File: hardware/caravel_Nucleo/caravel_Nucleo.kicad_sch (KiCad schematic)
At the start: 90 parts, among them J1 USB_B_Micro - 10118193-0001LF, J10 Conn_01x11_Female, J11 Conn_01x03, J12 Conn_01x02_Male, J2 Conn_01x02_Female, J3 Conn_01x02_Male, J4 Conn_01x04_Female, J5 Conn_01x02_Male, J6 Conn_01x02_Male, J7 Conn_01x06_Female, J8 Conn_01x03, J9 Conn_01x03, SW1 SW_Push - SKQGADE010, T1 Logo, T2 Logo, U1 FT232H, U10 MCP4661, U11 TAR5SxxU_SOT353F, U12 NUCLEO144-F429ZI, U2 SN74LVC1G125DCKR, U3 SN74LVC1G125DCKR, U4 MCP1319MT-29LE-OT, U5 TAR5SxxU_SOT353F, U6 TAR5SxxU_SOT353F, U7 W25Q32FVSS, U8 caravel_breakout, U9 MIC2211-AAYML-TR, X1 DSC6001_10MHZ, Y1 CSTNE12M0GH5L000R0

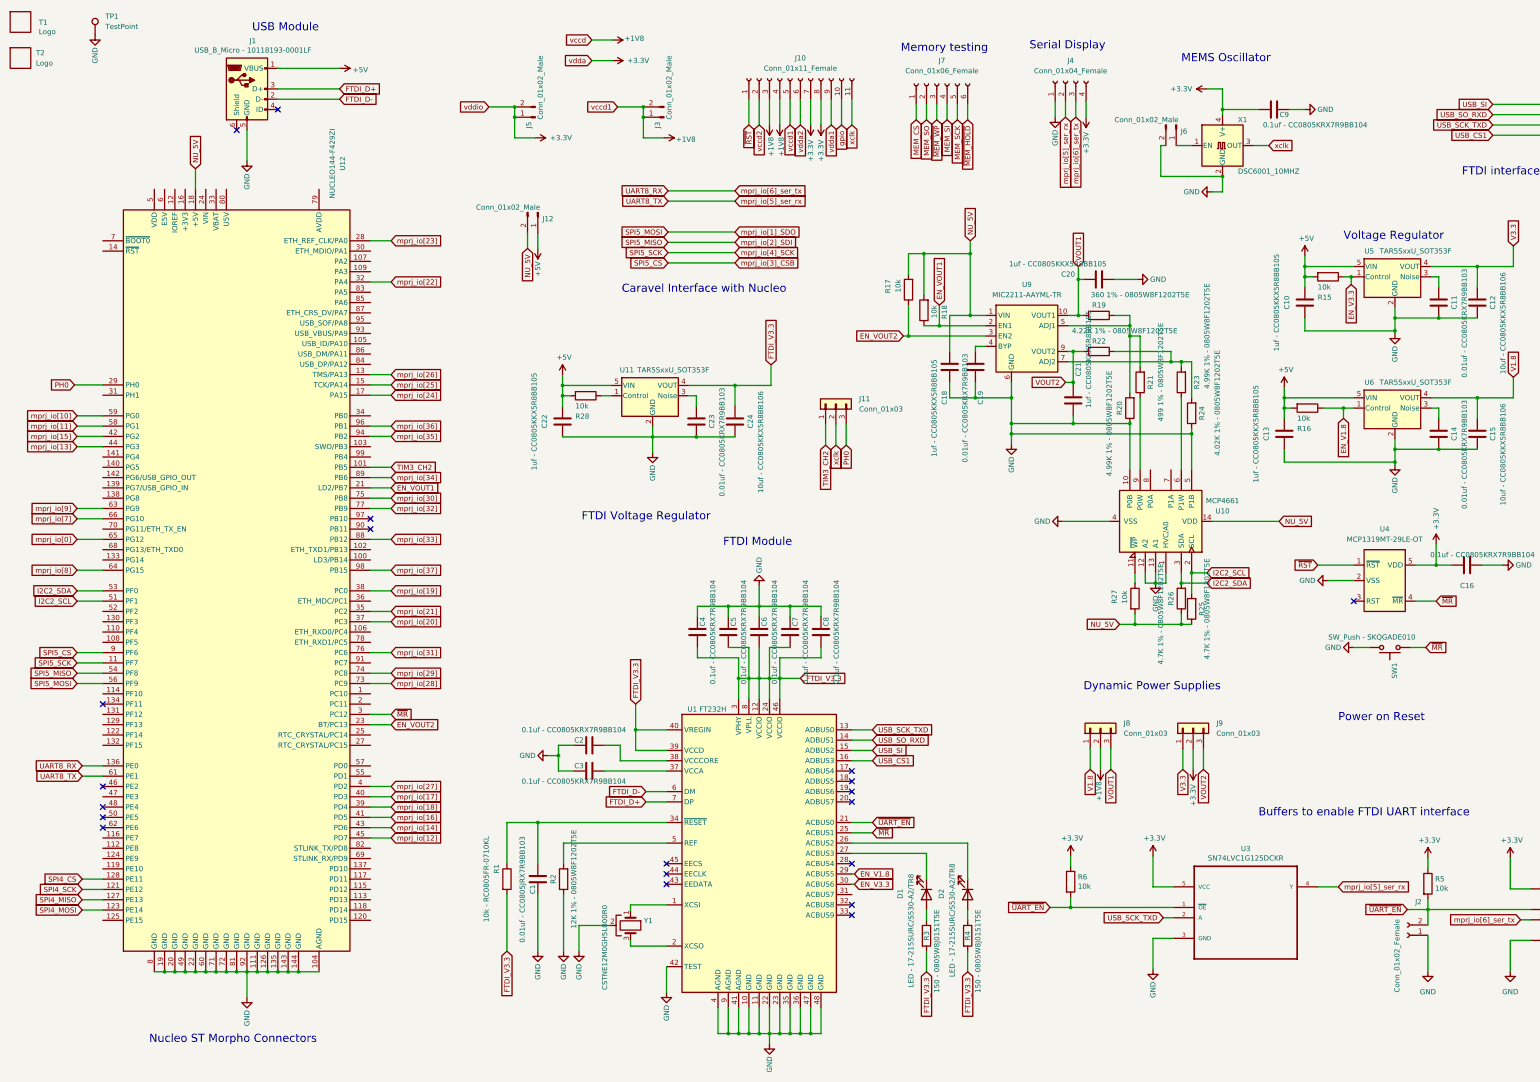
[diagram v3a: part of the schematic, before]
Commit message: update caravel nucleo hat board Rev A PCB
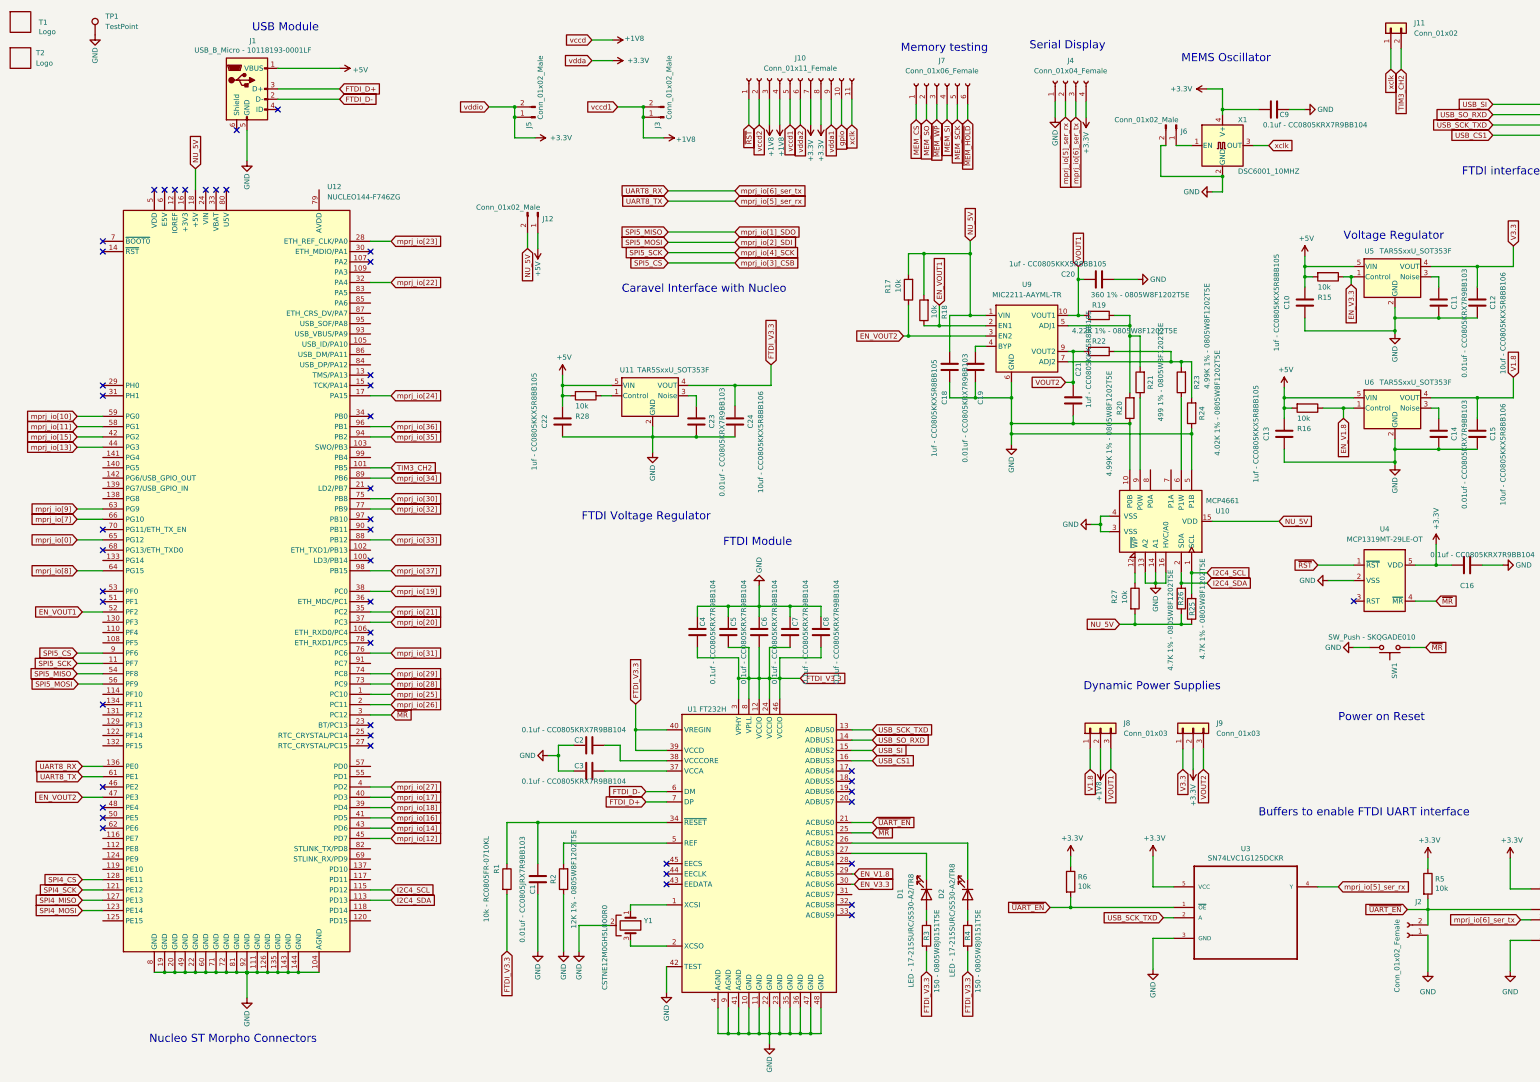
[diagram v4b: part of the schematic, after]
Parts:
- removed J11: Conn_01x03, Connector_PinHeader_2.54mm:PinHeader_1x03_P2.54mm_Vertical, symbol Connector_Generic:Conn_01x03
- removed U12: NUCLEO144-F429ZI, Caravel_Board:ST_Morpho_Connectors_144, symbol Caravel_board:NUCLEO144-F429ZI
- added J11: Conn_01x02, Connector_PinHeader_2.54mm:PinHeader_1x02_P2.54mm_Vertical, symbol Connector_Generic:Conn_01x02
- added U12: NUCLEO144-F746ZG, Module:ST_Morpho_Connector_144_STLink, symbol MCU_Module:NUCLEO144-F746ZG
- U10: footprint Caravel_Board:QFN-16-1EP_4x4mm_P0.65mm_EP2.5x2.5mm -> Package_DFN_QFN:QFN-16-1EP_5x5mm_P0.8mm_EP2.7x2.7mm
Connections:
- net EN_VOUT1: now also U12.52 (PF2)
- net EN_VOUT2: now also U12.47 (PE3)
- net GND: now also U10.14 (A1), U10.16 (HVC/A0), U10.3 (VSS), U12.104 (AGND), U12.111 (GND), U12.126 (GND), U12.135 (GND), U12.143 (GND), U12.144 (GND), U12.19 (GND), U12.20 (GND), U12.22 (GND), U12.49 (GND), U12.60 (GND), U12.71 (GND), U12.72 (GND), U12.8 (GND), U12.81 (GND), U12.92 (GND); no longer U10.1 (HVC/A0), U10.12 (A2)
- net NU_5V: now also U10.15 (VDD), U12.18 (+5V); no longer U10.14 (VDD)
- net SPI4_CS: now also U12.128 (PE11)
- net SPI4_MISO: now also U12.127 (PE13)
- net SPI4_MOSI: now also U12.123 (PE14)
- net SPI4_SCK: now also U12.121 (PE12)
- net SPI5_CS: now also U12.9 (PF6)
- net SPI5_MISO: now also U1.15 (ADBUS2), U8.41 (mprj_io[1]_SDO), U12.54 (PF8); no longer U1.14 (ADBUS1), U2.4 (Y), U8.40 (mprj_io[2]_SDI)
- net SPI5_MOSI: now also U1.14 (ADBUS1), U2.4 (Y), U8.40 (mprj_io[2]_SDI), U12.56 (PF9); no longer U1.15 (ADBUS2), U8.41 (mprj_io[1]_SDO)
- net SPI5_SCK: now also U12.11 (PF7)
- net TIM3_CH2: now also J11.2 (Pin_2), U12.101 (PB5)
- net UART8_RX: now also U12.136 (PE0)
- net UART8_TX: now also U12.61 (PE1)
- net mprj_io[0]: now also U12.65 (PG12)
- net mprj_io[10]: now also U12.59 (PG0)
- net mprj_io[11]: now also U12.58 (PG1)
- net mprj_io[12]: now also U12.45 (PD7)
- net mprj_io[13]: now also U12.44 (PG3)
- net mprj_io[14]: now also U12.43 (PD6)
- net mprj_io[15]: now also U12.42 (PG2)
- net mprj_io[16]: now also U12.41 (PD5)
- net mprj_io[17]: now also U12.40 (PD3)
- net mprj_io[18]: now also U12.39 (PD4)
- net mprj_io[19]: now also U12.38 (PC0)
- net mprj_io[20]: now also U12.37 (PC3)
- net mprj_io[21]: now also U12.35 (PC2)
- net mprj_io[22]: now also U12.32 (PA4)
- net mprj_io[23]: now also U12.28 (ETH_REF_CLK/PA0)
- net mprj_io[24]: now also U12.17 (PA15)
- net mprj_io[25]: now also U12.1 (PC10)
- net mprj_io[26]: now also U12.2 (PC11)
- net mprj_io[27]: now also U12.4 (PD2)
- net mprj_io[28]: now also U12.73 (PC9)
- net mprj_io[29]: now also U12.74 (PC8)
- net mprj_io[30]: now also U12.75 (PB8)
- net mprj_io[31]: now also U12.76 (PC6)
- net mprj_io[32]: now also U12.77 (PB9)
- net mprj_io[33]: now also U12.88 (PB12)
- net mprj_io[34]: now also U12.89 (PB6)
- net mprj_io[35]: now also U12.94 (PB2)
- net mprj_io[36]: now also U12.96 (PB1)
- net mprj_io[37]: now also U12.98 (PB15)
- net mprj_io[7]: now also U12.66 (PG10)
- net mprj_io[8]: now also U12.64 (PG15)
- net mprj_io[9]: now also U12.63 (PG9)
- net xclk: now also J11.1 (Pin_1)
- net ~{MR}: now also U12.3 (PC12)
- net at U10.11 (NC): no longer R27.1
- net I2C2_SCL renamed I2C4_SCL
- net I2C4_SCL: now also U10.1 (SCL), U12.115 (PD12); no longer U10.2 (SCL)
- net I2C2_SDA renamed I2C4_SDA
- net I2C4_SDA: now also U10.2 (SDA), U12.113 (PD13); no longer U10.3 (SDA)
- new net: R27.1, U10.12 (~{WP})
- no-connect marks 20 -> 48

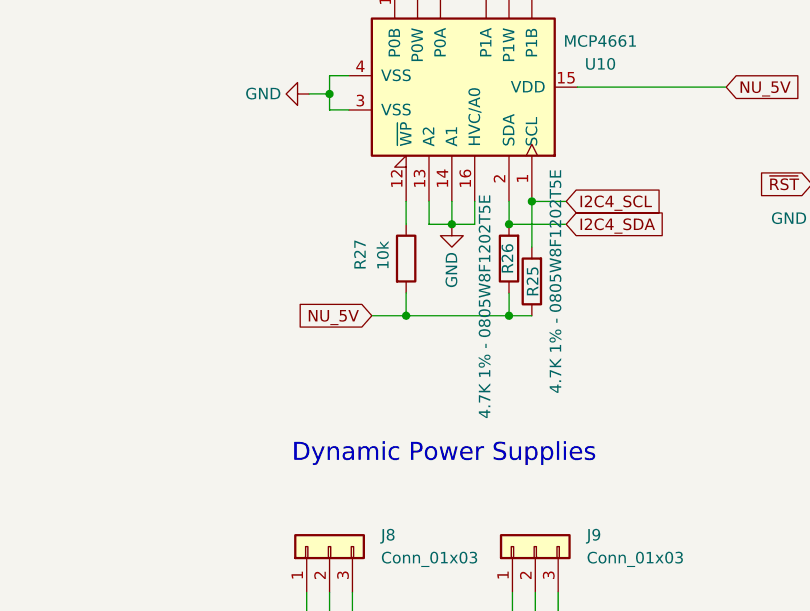
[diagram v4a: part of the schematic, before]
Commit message: update gpio_config_builder.py and gpio_config_io.c to not generate n_bits value
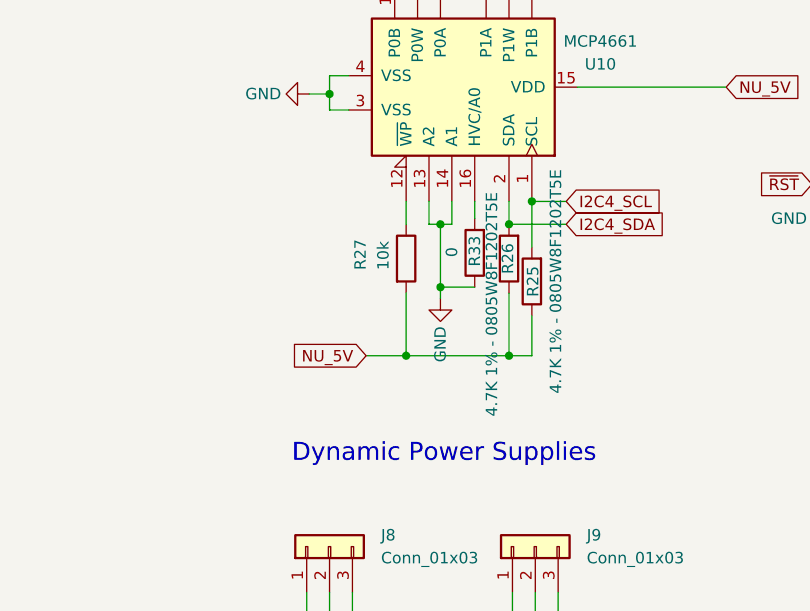
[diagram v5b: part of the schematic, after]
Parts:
- added R33: 0, Resistor_SMD:R_0805_2012Metric, symbol Device:R
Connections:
- net GND: now also R33.1; no longer U10.16 (HVC/A0)
- new net: R33.2, U10.16 (HVC/A0)
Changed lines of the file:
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@@
   (junction (at 438.785 177.8) (diameter 0) (color 0 0 0 0)
   )
-  (junction (at 302.895 166.37) (diameter 0) (color 0 0 0 0)
+  (junction (at 302.895 170.815) (diameter 0) (color 0 0 0 0)
   )
   (junction (at 260.985 119.38) (diameter 0) (color 0 0 0 0)
@@
   (junction (at 211.455 267.335) (diameter 0) (color 0 0 0 0)
   )
-  (junction (at 291.465 166.37) (diameter 0) (color 0 0 0 0)
+  (junction (at 291.465 170.815) (diameter 0) (color 0 0 0 0)
   )
   (junction (at 290.195 116.84) (diameter 0) (color 0 0 0 0)
@@
   (junction (at 431.165 175.26) (diameter 0) (color 0 0 0 0)
   )
-  (junction (at 296.545 156.21) (diameter 0) (color 0 0 0 0)
-  )
   (junction (at 80.01 252.222) (diameter 0) (color 0 0 0 0)
   )
@@
   (junction (at 300.355 101.6) (diameter 0) (color 0 0 0 0)
   )
+  (junction (at 295.275 163.195) (diameter 0) (color 0 0 0 0)
+  )
   (junction (at 191.135 267.335) (diameter 0) (color 0 0 0 0)
   )
@@
   (junction (at 375.92 110.49) (diameter 0) (color 0 0 0 0)
   )
+  (junction (at 295.275 156.21) (diameter 0) (color 0 0 0 0)
+  )
   (junction (at 366.395 123.19) (diameter 0) (color 0 0 0 0)
   )
@@
     (stroke (width 0) (type default) (color 0 0 0 0))
   )
-  (wire (pts (xy 294.005 153.67) (xy 294.005 156.21))
+  (wire (pts (xy 295.275 156.21) (xy 296.545 156.21))
+    (stroke (width 0) (type default) (color 0 0 0 0))
+  )
+  (wire (pts (xy 299.085 153.67) (xy 299.085 155.575))
     (stroke (width 0) (type default) (color 0 0 0 0))
   )
@@
     (stroke (width 0) (type default) (color 0 0 0 0))
   )
+  (wire (pts (xy 295.275 156.21) (xy 295.275 163.195))
+    (stroke (width 0) (type default) (color 0 0 0 0))
+  )
   (wire (pts (xy 441.325 43.18) (xy 441.325 38.1))
     (stroke (width 0) (type default) (color 0 0 0 0))
@@
     (stroke (width 0) (type default) (color 0 0 0 0))
   )
-  (wire (pts (xy 287.655 166.37) (xy 291.465 166.37))
+  (wire (pts (xy 287.02 170.815) (xy 291.465 170.815))
     (stroke (width 0) (type default) (color 0 0 0 0))
   )
@@
     (stroke (width 0) (type default) (color 0 0 0 0))
   )
-  (wire (pts (xy 299.085 153.67) (xy 299.085 156.21))
-    (stroke (width 0) (type default) (color 0 0 0 0))
-  )
   (wire (pts (xy 192.786 74.676) (xy 176.276 74.676))
     (stroke (width 0) (type default) (color 0 0 0 0))
@@
     (stroke (width 0) (type default) (color 0 0 0 0))
   )
+  (wire (pts (xy 295.275 164.465) (xy 295.275 163.195))
+    (stroke (width 0) (type default) (color 0 0 0 0))
+  )
   (wire (pts (xy 446.405 180.34) (xy 446.405 189.23))
     (stroke (width 0) (type default) (color 0 0 0 0))
@@
     (stroke (width 0) (type default) (color 0 0 0 0))
   )
-  (wire (pts (xy 296.545 153.67) (xy 296.545 156.21))
-    (stroke (width 0) (type default) (color 0 0 0 0))
-  )
   (wire (pts (xy 80.01 252.222) (xy 82.55 252.222))
     (stroke (width 0) (type default) (color 0 0 0 0))
@@
     (stroke (width 0) (type default) (color 0 0 0 0))
   )
-  (wire (pts (xy 302.895 166.37) (xy 305.435 166.37))
-    (stroke (width 0) (type default) (color 0 0 0 0))
-  )
   (wire (pts (xy 150.241 120.142) (xy 172.466 120.142))
     (stroke (width 0) (type default) (color 0 0 0 0))
@@
     (stroke (width 0) (type default) (color 0 0 0 0))
   )
+  (wire (pts (xy 294.005 153.67) (xy 294.005 156.21))
+    (stroke (width 0) (type default) (color 0 0 0 0))
+  )
   (wire (pts (xy 102.87 153.162) (xy 107.95 153.162))
     (stroke (width 0) (type default) (color 0 0 0 0))
@@
     (stroke (width 0) (type default) (color 0 0 0 0))
   )
-  (wire (pts (xy 294.005 156.21) (xy 296.545 156.21))
-    (stroke (width 0) (type default) (color 0 0 0 0))
-  )
   (wire (pts (xy 471.805 43.18) (xy 471.805 38.1))
     (stroke (width 0) (type default) (color 0 0 0 0))
@@
     (stroke (width 0) (type default) (color 0 0 0 0))
   )
-  (wire (pts (xy 291.465 163.83) (xy 291.465 166.37))
+  (wire (pts (xy 291.465 163.83) (xy 291.465 170.815))
     (stroke (width 0) (type default) (color 0 0 0 0))
   )
@@
     (stroke (width 0) (type default) (color 0 0 0 0))
   )
-  (wire (pts (xy 296.545 156.21) (xy 299.085 156.21))
-    (stroke (width 0) (type default) (color 0 0 0 0))
-  )
   (wire (pts (xy 107.95 178.562) (xy 102.87 178.562))
     (stroke (width 0) (type default) (color 0 0 0 0))
@@
     (stroke (width 0) (type default) (color 0 0 0 0))
   )
+  (wire (pts (xy 296.545 156.21) (xy 296.545 153.67))
+    (stroke (width 0) (type default) (color 0 0 0 0))
+  )
   (wire (pts (xy 183.515 161.925) (xy 183.515 164.465))
     (stroke (width 0) (type default) (color 0 0 0 0))
@@
     (stroke (width 0) (type default) (color 0 0 0 0))
   )
-  (wire (pts (xy 302.895 163.83) (xy 302.895 166.37))
+  (wire (pts (xy 302.895 163.83) (xy 302.895 170.815))
     (stroke (width 0) (type default) (color 0 0 0 0))
   )
@@
     (stroke (width 0) (type default) (color 0 0 0 0))
   )
+  (wire (pts (xy 294.005 156.21) (xy 295.275 156.21))
+    (stroke (width 0) (type default) (color 0 0 0 0))
+  )
   (wire (pts (xy 36.83 203.962) (xy 31.75 203.962))
     (stroke (width 0) (type default) (color 0 0 0 0))
@@
     (stroke (width 0) (type default) (color 0 0 0 0))
   )
-  (wire (pts (xy 291.465 166.37) (xy 302.895 166.37))
+  (wire (pts (xy 291.465 170.815) (xy 302.895 170.815))
     (stroke (width 0) (type default) (color 0 0 0 0))
   )
@@
     (stroke (width 0) (type default) (color 0 0 0 0))
   )
+  (wire (pts (xy 305.435 170.815) (xy 302.895 170.815))
+    (stroke (width 0) (type default) (color 0 0 0 0))
+  )
   (wire (pts (xy 485.775 182.88) (xy 485.775 189.23))
     (stroke (width 0) (type default) (color 0 0 0 0))
@@
     (stroke (width 0) (type default) (color 0 0 0 0))
   )
+  (wire (pts (xy 305.435 166.37) (xy 305.435 170.815))
+    (stroke (width 0) (type default) (color 0 0 0 0))
+  )
   (wire (pts (xy 302.895 156.21) (xy 309.245 156.21))
     (stroke (width 0) (type default) (color 0 0 0 0))
@@
     (stroke (width 0) (type default) (color 0 0 0 0))
   )
+  (wire (pts (xy 299.085 163.195) (xy 295.275 163.195))
+    (stroke (width 0) (type default) (color 0 0 0 0))
+  )
   (wire (pts (xy 443.865 115.57) (xy 443.865 111.76))
     (stroke (width 0) (type default) (color 0 0 0 0))
@@
     )
   )
-  (global_label "NU_5V" (shape input) (at 287.655 166.37 180) (fields_autoplaced)
+  (global_label "NU_5V" (shape input) (at 287.02 170.815 180) (fields_autoplaced)
     (effects (font (size 1.27 1.27)) (justify right))
-    (property "Intersheet References" "${INTERSHEET_REFS}" (id 0) (at 279.3152 166.4494 0)
+    (property "Intersheet References" "${INTERSHEET_REFS}" (id 0) (at 278.6802 170.8944 0)
       (effects (font (size 1.27 1.27)) (justify right) hide)
     )
@@
     (in_bom yes) (on_board yes)
     (property "Reference" "R26" (id 0) (at 302.768 160.02 90))
-    (property "Value" "4.7K 1% - 0805W8F1202T5E" (id 1) (at 300.228 165.354 90))
+    (property "Value" "4.7K 1% - 0805W8F1202T5E" (id 1) (at 300.99 165.1 90))
     (property "Footprint" "Resistor_SMD:R_0805_2012Metric" (id 2) (at 304.673 160.02 90)
       (effects (font (size 1.27 1.27)) hide)
@@
     (pin "2")
   )
-  (symbol (lib_id "power:GND") (at 296.545 156.21 0) (unit 1)
+  (symbol (lib_id "power:GND") (at 295.275 164.465 0) (unit 1)
     (in_bom yes) (on_board yes)
-    (property "Reference" "#PWR0118" (id 0) (at 296.545 162.56 0)
+    (property "Reference" "#PWR0118" (id 0) (at 295.275 170.815 0)
       (effects (font (size 1.27 1.27)) hide)
     )
-    (property "Value" "GND" (id 1) (at 296.545 161.29 90))
-    (property "Footprint" "" (id 2) (at 296.545 156.21 0)
+    (property "Value" "GND" (id 1) (at 295.275 169.545 90))
+    (property "Footprint" "" (id 2) (at 295.275 164.465 0)
       (effects (font (size 1.27 1.27)) hide)
     )
-    (property "Datasheet" "" (id 3) (at 296.545 156.21 0)
+    (property "Datasheet" "" (id 3) (at 295.275 164.465 0)
       (effects (font (size 1.27 1.27)) hide)
     )
@@
     (pin "2")
   )
+  (symbol (lib_id "Device:R") (at 299.085 159.385 180) (unit 1)
+    (in_bom yes) (on_board yes)
+    (property "Reference" "R33" (id 0) (at 299.085 157.48 90)
+      (effects (font (size 1.27 1.27)) (justify left))
+    )
+    (property "Value" "0" (id 1) (at 296.545 158.75 90)
+      (effects (font (size 1.27 1.27)) (justify left))
+    )
+    (property "Footprint" "Resistor_SMD:R_0805_2012Metric" (id 2) (at 300.863 159.385 90)
+      (effects (font (size 1.27 1.27)) hide)
+    )
+    (property "Datasheet" "~" (id 3) (at 299.085 159.385 0)
+      (effects (font (size 1.27 1.27)) hide)
+    )
+    (pin "1")
+    (pin "2")
+  )
   (symbol (lib_id "Device:R") (at 501.015 193.04 0) (unit 1)
     (in_bom yes) (on_board yes)
@@
       (reference "R32") (unit 1) (value "0") (footprint "Resistor_SMD:R_0805_2012Metric")
     )
+    (path "/81219724-582f-4ecc-a604-71c45712c85d"
+      (reference "R33") (unit 1) (value "0") (footprint "Resistor_SMD:R_0805_2012Metric")
+    )
     (path "/9df1a424-88bb-423b-b45f-28cb02f1489c"
